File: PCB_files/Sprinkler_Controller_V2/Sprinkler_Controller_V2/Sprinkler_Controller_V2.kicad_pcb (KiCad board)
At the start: 2 copper layers, 116 x 72 mm, 42 parts, among them J1 Screw_Terminal_01x02, J2 Screw_Terminal_01x11, U1 ESP32_DevKit_V1_DOIT, U12 TPP362081-T6TR

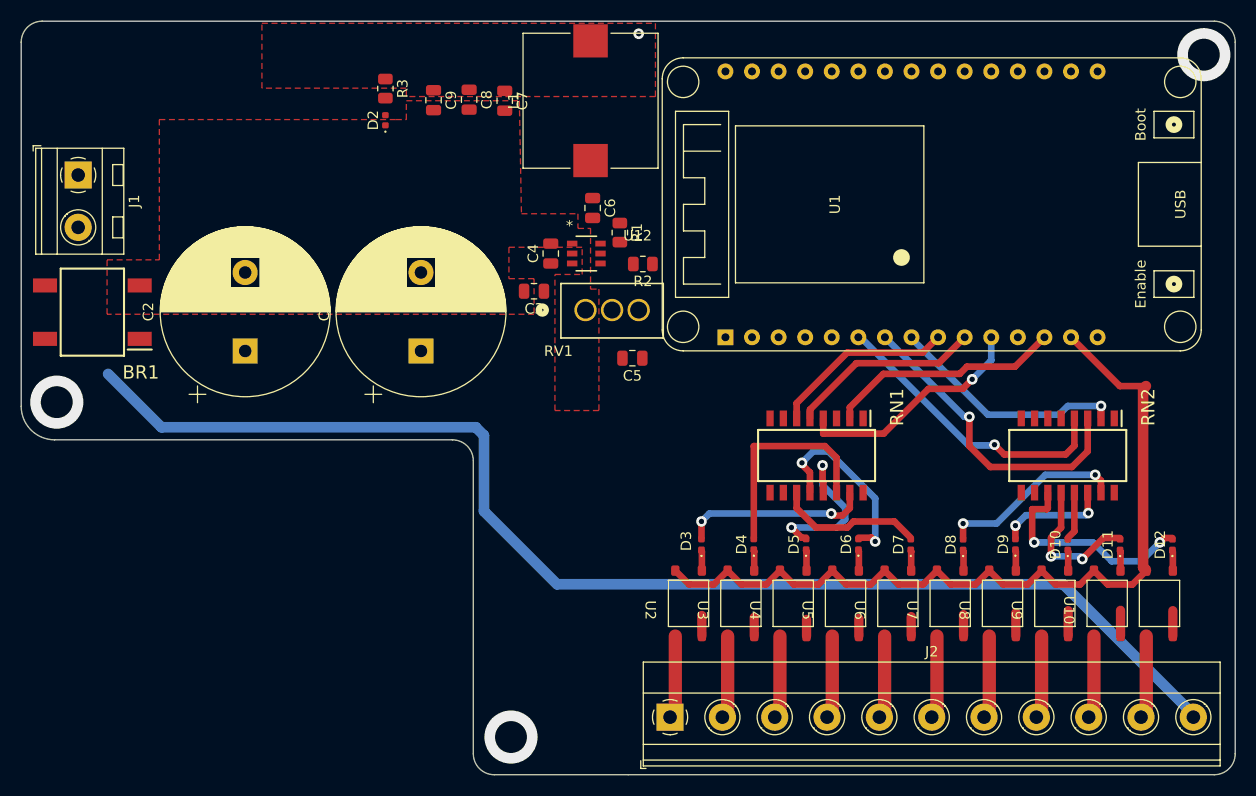
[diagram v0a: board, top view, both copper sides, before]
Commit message: PCB_v2 added pours
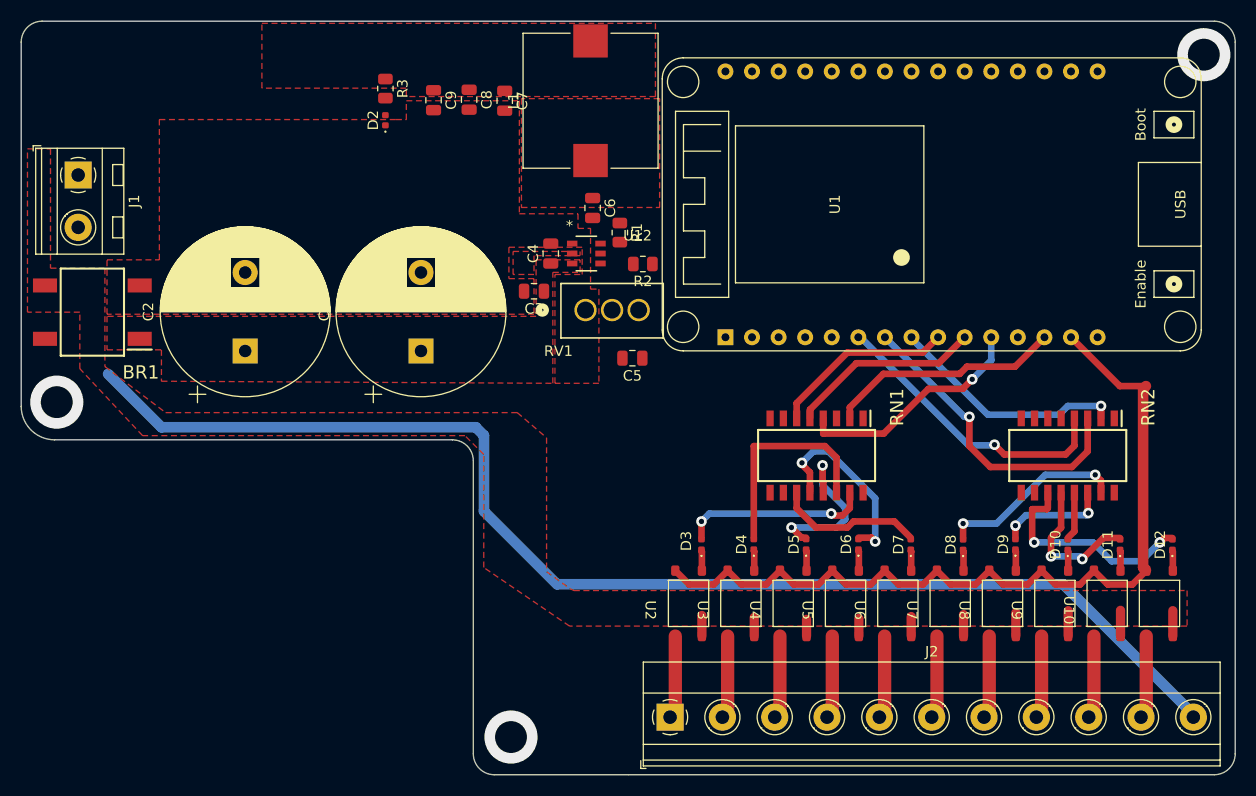
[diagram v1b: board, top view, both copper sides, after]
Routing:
- net (no net): vias 4 -> 3
- added copper zone on F.Cu, net /Vin
- added copper zone on F.Cu, net AC
- added copper zone on F.Cu, net SW
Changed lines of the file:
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@@
-	)
-	(via
-		(at 156 81.2)
-		(size 1.016)
-		(drill 0.508)
-		(layers "F.Cu" "B.Cu")
-		(net 0)
 	)
 	(via
@@
 	)
 	(zone
+		(net 76)
+		(net_name "SW")
+		(layer "F.Cu")
+		(hatch edge 0.5)
+		(priority 3)
+		(connect_pads
+			(clearance 0.5)
+		)
+		(min_thickness 0.25)
+		(filled_areas_thickness no)
+		(fill yes
+			(thermal_gap 0.5)
+			(thermal_bridge_width 0.5)
+		)
+		(polygon
+			(pts
+				(xy 144 104.2) (xy 144 102) (xy 150.4 102) (xy 150.4 102.4) (xy 146 102.4) (xy 146 104.2)
+			)
+		)
+	)
+	(zone
 		(net 67)
 		(net_name "GND")
@@
 		(min_thickness 0.25)
 		(filled_areas_thickness no)
-		(fill
+		(fill yes
 			(thermal_gap 0.5)
 			(thermal_bridge_width 0.5)
@@
 			(pts
 				(xy 105.2 102.8) (xy 110.2 102.8) (xy 110.2 89.4) (xy 132.8 89.4) (xy 133.8 89.4) (xy 133.8 87.6)
-				(xy 144.6 87.6) (xy 144.8 98.4) (xy 150.2 98.4) (xy 150.2 99.8) (xy 151.4 99.8) (xy 151.4 105.6)
-				(xy 152.2 105.6) (xy 152.2 117.2) (xy 148 117.2) (xy 148 104.2) (xy 150.6 104.2) (xy 150.6 101.6)
+				(xy 144.6 87.6) (xy 144.6 98.4) (xy 150.2 98.4) (xy 150.2 99.8) (xy 151.4 99.8) (xy 151.4 105.6)
+				(xy 152.2 105.6) (xy 152.2 114.6) (xy 148 114.6) (xy 148 104.2) (xy 150.6 104.2) (xy 150.6 101.6)
 				(xy 143.6 101.6) (xy 143.6 104.6) (xy 146 104.6) (xy 146 108) (xy 105.2 108)
 			)
@@
 		(min_thickness 0.25)
 		(filled_areas_thickness no)
-		(fill
+		(fill yes
 			(thermal_gap 0.5)
 			(thermal_bridge_width 0.5)
@@
 			)
 		)
+	)
+	(zone
+		(net 76)
+		(net_name "SW")
+		(layer "F.Cu")
+		(hatch edge 0.5)
+		(priority 5)
+		(connect_pads
+			(clearance 0.5)
+		)
+		(min_thickness 0.25)
+		(filled_areas_thickness no)
+		(fill yes
+			(thermal_gap 0.5)
+			(thermal_bridge_width 0.5)
+		)
+		(polygon
+			(pts
+				(xy 158 87.4) (xy 144.8 87.4) (xy 144.8 97.8) (xy 158 97.8)
+			)
+		)
+	)
+	(zone
+		(net 78)
+		(net_name "AC")
+		(layer "F.Cu")
+		(hatch edge 0.5)
+		(priority 4)
+		(connect_pads
+			(clearance 0.5)
+		)
+		(min_thickness 0.25)
+		(filled_areas_thickness no)
+		(fill yes
+			(thermal_gap 0.5)
+			(thermal_bridge_width 0.5)
+		)
+		(polygon
+			(pts
+				(xy 97.6 107.8) (xy 97.6 92.2) (xy 99.8 92.2) (xy 99.8 103.6) (xy 105 103.6) (xy 105 113) (xy 110.8 117.4)
+				(xy 144.4 117.4) (xy 147.2 119.8) (xy 147.2 132.6) (xy 149.4 134.2) (xy 149.8 134.4) (xy 208.4 134.4)
+				(xy 208.4 137.8) (xy 149.4 137.8) (xy 141.2 132.2) (xy 141.2 121.4) (xy 139.4 119.6) (xy 108.6 119.6)
+				(xy 102.6 113.2) (xy 102.6 107.8)
+			)
+		)
+	)
+	(zone
+		(net 8)
+		(net_name "/Vin")
+		(layer "F.Cu")
+		(hatch edge 0.5)
+		(priority 2)
+		(connect_pads
+			(clearance 0.5)
+		)
+		(min_thickness 0.25)
+		(filled_areas_thickness no)
+		(fill yes
+			(thermal_gap 0.5)
+			(thermal_bridge_width 0.5)
+		)
+		(polygon
+			(pts
+				(xy 105.2 111.4) (xy 110.4 111.4) (xy 110.4 114.4) (xy 147.8 114.6) (xy 147.8 104) (xy 150.4 104)
+				(xy 150.4 102.8) (xy 146.2 102.8) (xy 146.2 108.2) (xy 105.2 108.2)
+			)
+		)

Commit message: V2 PCB Complete
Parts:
- added SW1: SW_SPST, Connector_PinHeader_2.54mm:PinHeader_1x02_P2.54mm_Vertical, F.Cu at (102.1, 87.8)
- moved C1 16.8 mm to (118.4, 111.5)
- moved C2 16.8 mm to (135.2, 111.5)
- moved C8 0.40 mm to (139.4, 87.5)
- moved C9 0.40 mm to (136.0, 87.5)
- moved L1 0.40 mm to (151.4, 88.0)
- moved C7 0.40 mm to (142.8, 87.6)
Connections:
- J1 pad 1: AC -> AC_to_SW
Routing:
- net VCC: track 0.00 -> 50.9 mm, vias 0 -> 2
- net Net-(U1-IO18): track 0.00 -> 48.0 mm, vias 0 -> 2
- net Net-(U1-IO19): track 0.00 -> 41.2 mm
- net Net-(U1-IO21): track 0.00 -> 36.2 mm, vias 0 -> 2
- net GNDPWR: track 122.3 -> 145.4 mm, vias 0 -> 1
- net AC: track 20.5 -> 39.2 mm
- net FB: track 0.00 -> 9.92 mm
- net Net-(C5-Pad1): track 0.00 -> 9.36 mm
- net AC_to_SW: track 0.00 -> 8.66 mm
- net SW: track 0.00 -> 3.25 mm, vias 0 -> 15
- net Net-(C6-Pad2): track 0.00 -> 2.80 mm
- net BOOT: track 0.00 -> 1.90 mm
- net Net-(D2-A): track 0.00 -> 1.63 mm
- net Net-(U1-IO25): track 22.8 -> 22.0 mm
- net GND: track 81.9 -> 81.3 mm, vias 0 -> 33
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- added copper zone on B.Cu, net AC_to_SW
- added copper zone on F.Cu, net AC_to_SW
- added copper zone on B.Cu, net GND
- added copper zone on B.Cu, net SW
